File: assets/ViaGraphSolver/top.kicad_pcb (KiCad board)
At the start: 2 copper layers, 0 parts

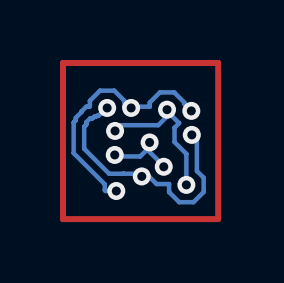
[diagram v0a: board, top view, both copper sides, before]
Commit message: Added new convex via topology
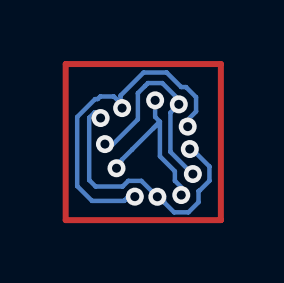
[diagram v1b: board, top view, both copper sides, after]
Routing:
- net Net5: track 2.63 -> 6.12 mm
- net Net6: track 8.94 -> 11.3 mm
- net Net7: track 5.59 -> 7.25 mm

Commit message: patch
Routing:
- net Net6: track 11.3 -> 10.7 mm

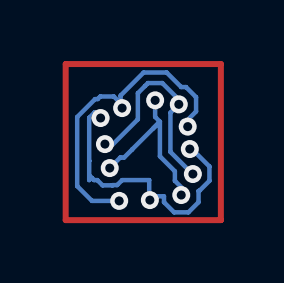
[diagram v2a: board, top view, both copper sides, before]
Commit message: Fix via-region over-porting and incorrect trace visualization by limiting via ports to 4 sides and resolving solved routes into top stubs + tile-scoped bottom segments
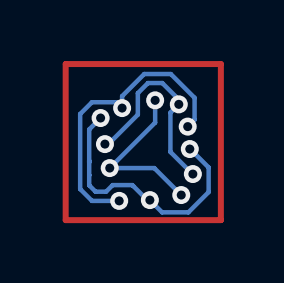
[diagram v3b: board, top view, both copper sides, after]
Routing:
- net Net8: track 9.96 -> 9.07 mm
- net Net5: track 6.28 -> 5.64 mm
- net Net6: track 10.7 -> 10.1 mm

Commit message: Optimize Default Via Topology for  Improved Solve Performance
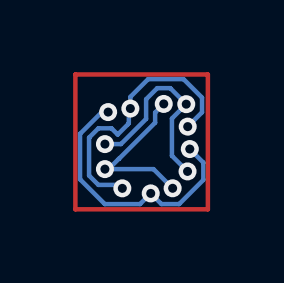
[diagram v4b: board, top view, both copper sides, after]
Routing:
- net Net6: track 10.1 -> 9.21 mm
